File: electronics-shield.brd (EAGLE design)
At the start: 65 x 56 mm, 104 parts, among them IC1 TLE9201SG, IC2 TLE9201SG, IC3 TLE9201SG, IC4 TLE9201SG, IC6 AOZ1232QI-01, IC8 AOZ1232QI-01, Q2 IRFR5305, U1 STM32F0XX8T, U2 EEPROM-I2C, U3 MAXIM_DS3231MZ+MAXIM_DS3231MZ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, U4 V_REG_317SMD, X1 CONNECTOR_PHOENIX_3.81, X2 Listwa zaciskowa rozłączalna 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, X3 C-GRID-04-70553, Y2 8MHz

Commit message: Removed unnecessary stuff, cleaning
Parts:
- removed BT1: 6.8MM_COIN_CELL, SparkFun-Batteries:BATTCON-6.8MM
- removed C18, C25: 22uF/35V, rcl:PANASONIC_B
- removed C20, C26: (no value), Kell Ideas:C0603K
- removed C21, C27, C31, C32: 33uF/10V, rcl:PANASONIC_B
- removed C22, C28: 100n, Kell Ideas:C0603K
- removed C23, C29: 1nF, Kell Ideas:C0603K
- removed C24, C30: 1uF/35V, Kell Ideas:C0603K
- removed IC6, IC8: AOZ1232QI-01, Kell Ideas:AOZ1232QI01
- removed L2, L3: 1uH, rcl:L4532P
- removed R11, R16: 65k, Kell Ideas:R0603
- removed R14, R21: 10k, Kell Ideas:R0603
- removed R15, R22: 100k, Kell Ideas:R0603
- removed R17, R18, R19, R20: (no value), Kell Ideas:R0603
- removed R23, R24: 456, Kell Ideas:R0603
- removed U2: EEPROM-I2C, Kell Ideas:SO-08
- removed U3: MAXIM_DS3231MZ+MAXIM_DS3231MZ+_0_0, Kell Ideas:MAXIM_DS3231MZ+_0
- removed X3: C-GRID-04-70553, con-molex:70553-04
- added U$1, U$2: POLOLU_D24V22FX, Kell Ideas:POLOLU_D24V22FX
- moved F3 5.79 mm to (32.0, 26.2)
- moved F5 2.62 mm to (19.8, 23.9), turned to 0 degrees
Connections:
- net UART_SELECTOR renamed SIGNAL_SELECTOR
- removed net BATTERY: BT1.+
- removed net BST1: C22.2, IC6.27
- removed net BST2: C28.2, IC8.27
- removed net FB1: IC6.5, R11.2, R14.1
- removed net FB2: IC8.5, R16.2, R21.1
- removed net LX2: C28.1, IC8.20, IC8.21, IC8.22, IC8.23, IC8.24, IC8.25, IC8.31, L3.1, R16.1
- removed net LX3: C22.1, IC6.20, IC6.21, IC6.22, IC6.23, IC6.24, IC6.25, IC6.31, L2.1, R11.1
- removed net N$2: R18.1
- removed net N$3: R17.1
- removed net PGOOD1: IC6.1, R15.2
- removed net PGOOD2: IC8.1, R22.2
- removed net SS1: C23.2, IC6.30
- removed net SS2: C29.2, IC8.30
- removed net TON1: IC6.6, R24.2
- removed net TON2: IC8.6, R23.2
- removed net VBAT: U3.6
- removed net VCC_INT1: C24.2, IC6.2, IC6.28, R15.1
- removed net VCC_INT2: C30.2, IC8.2, IC8.28, R22.1
- new net STM_RX: U1.43
- new net STM_TX: U1.42
- net +3V3: no longer C20.1, C26.2, R17.2, R18.2, R19.1, R20.1, U2.7, U2.8
- net +5V: now also U$2.P$5; no longer C27.+, C31.+, L3.2
- net DATA_N: no longer X3.3
- net DATA_P: no longer X3.2
- net GND: now also U$1.P$4, U$2.P$4; no longer BT1.-, C18.-, C20.2, C21.-, C23.1, C24.1, C25.-, C26.1, C27.-, C29.1, C30.1, C31.-, C32.-, IC6.12, IC6.13, IC6.14, IC6.15, IC6.16, IC6.17, IC6.18, IC6.19, IC6.26, IC6.29, IC6.32, IC6.4, IC8.12, IC8.13, IC8.14, IC8.15, IC8.16, IC8.17, IC8.18, IC8.19, IC8.26, IC8.29, IC8.32, IC8.4, R14.2, R21.2, U2.2, U2.3, U2.4, U3.5, X3.1
- net RPI_RXD: no longer U1.42
- net RPI_TXD: no longer U1.43
- net SCL: no longer R19.2, U1.35, U2.6
- net SDA: no longer R20.2, U1.36, U2.5
- net VCC: now also U$1.P$3, U$2.P$3; no longer C18.+, C25.+, IC6.10, IC6.11, IC6.33, IC6.7, IC6.8, IC6.9, IC8.10, IC8.11, IC8.33, IC8.7, IC8.8, IC8.9, R23.1, R24.1, U3.2
- net VCC_SERVO: now also U$1.P$5; no longer C21.+, C32.+, L2.2
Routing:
- net N$18: track 9.74 -> 47.4 mm, vias 0 -> 2
- net DATA_N: track 31.5 -> 0.00 mm
- net DATA_P: track 26.0 -> 0.00 mm
- net VCC: track 152.1 -> 176.2 mm
- net GND: track 23.3 -> 1.52 mm, vias 68 -> 62
- net SDA_RX: track 15.6 -> 0.00 mm
- net SCL: track 25.4 -> 10.6 mm
- net SCL_TX: track 14.6 -> 0.00 mm
- net SDA: track 28.0 -> 13.8 mm
- net VCC_INT2: track 11.3 -> 0.00 mm, vias 2 -> 0
- net VCC_INT1: track 11.3 -> 0.00 mm, vias 2 -> 0
- net VCC_SERVO: track 35.2 -> 46.1 mm
- net RPI_TXD: track 27.4 -> 19.4 mm
- net RPI_RXD: track 22.4 -> 14.7 mm
- net LX2: track 7.38 -> 0.00 mm, vias 2 -> 0
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- removed copper zone on layer 16, net +5V
- removed copper zone on layer 16, net LX2
- removed copper zone on layer 16, net LX3
- removed copper zone on layer 16, net VCC
- removed copper zone on layer 16, net VCC_SERVO
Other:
- board text added: "POLOLU D24V22Fx 5V"
- board text added: "POLOLU D24V22Fx 6V/9V/12V"
- board text added: "electronics-shield ver 8 2018 Kell ideas Ltd."
- board text removed: "electronics-shield ver 8 rev A 2018 Kell ideas Ltd."

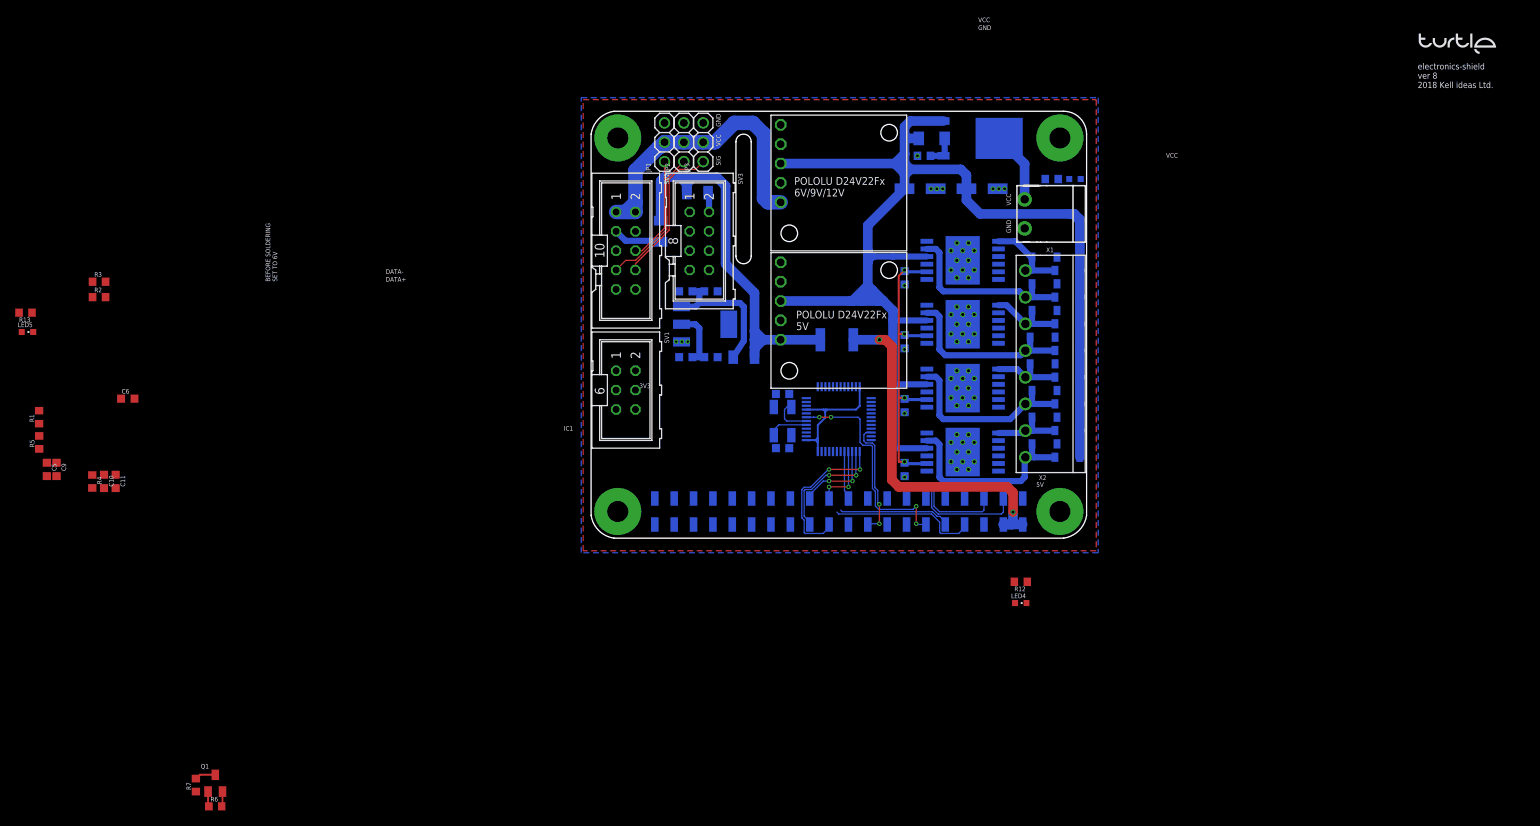
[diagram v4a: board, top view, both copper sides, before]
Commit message: Basic placement of rest of components
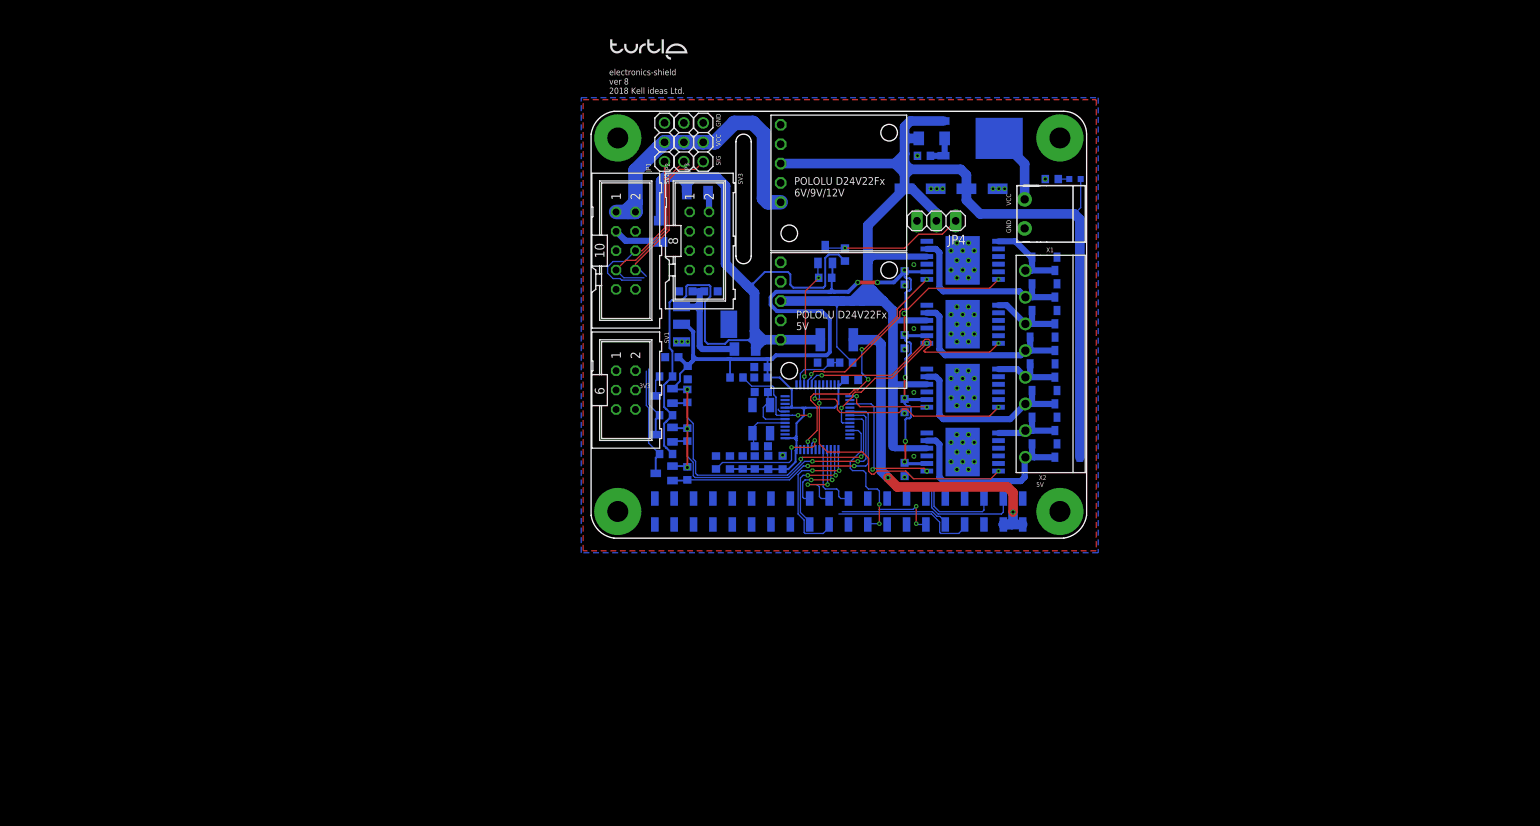
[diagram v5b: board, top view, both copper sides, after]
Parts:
- removed LED4, LED5: LEDCHIPLED_0603, audio amplifier example:CHIPLED_0603
- added JP4: (no value), pinhead:1X03
- added Q3, Q4, Q5: (no value), adafruit:SOT23
- added R10, R11, R14, R15, R16, R17: 10k, rcl:R0603
- moved R13 105.0 mm to (30.3, 23.2), flipped to the bottom, turned to 0 degrees
- moved C9 95.3 mm to (24.9, 10.1), flipped to the bottom, turned to 90 degrees
- moved C6 95.0 mm to (33.9, 20.9), flipped to the bottom, turned to 180 degrees
- moved C5 94.6 mm to (23.0, 10.1), flipped to the bottom, turned to 90 degrees
- moved R1 94.1 mm to (21.2, 10.1), flipped to the bottom, turned to 270 degrees
- moved R5 88.8 mm to (16.2, 10.1), flipped to the bottom, turned to 270 degrees
- moved R3 87.7 mm to (19.7, 10.1), flipped to the bottom, turned to 270 degrees
- moved C10 87.5 mm to (22.0, 22.6), flipped to the bottom, turned to 0 degrees
- moved C11 85.7 mm to (22.0, 21.2), flipped to the bottom, turned to 0 degrees
- moved R4 85.6 mm to (18.8, 21.2), flipped to the bottom, turned to 0 degrees
- moved R2 85.5 mm to (18.0, 10.1), flipped to the bottom, turned to 270 degrees
- moved R6 75.8 mm to (12.4, 8.64), flipped to the bottom, turned to 270 degrees
- moved R7 75.4 mm to (9.60, 11.2), flipped to the bottom, turned to 0 degrees
- moved Q1 71.5 mm to (9.35, 8.64), flipped to the bottom, turned to 270 degrees
- moved R12 36.8 mm to (33.2, 23.2), flipped to the bottom, turned to 0 degrees
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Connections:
- net DATA_N renamed NSS_1
- net DATA_P renamed NSS_2
- removed net N$4: LED4.C, R12.1
- removed net N$5: LED5.C, R13.1
- removed net SO1-SI3: IC1.3, IC3.8
- removed net SO2-SI4: IC2.3, IC4.8
- removed net SO3-SI2: IC2.8, IC3.3
- new net LED_5V: JP4.1, Q5.3, R17.2
- net +3V3: now also Q3.1, Q4.1, Q5.1, R10.1, R14.1, R16.1; no longer LED5.A
- net +5V: now also R11.1, R15.1, R17.1; no longer LED4.A
- net BAT_MEAS: now also R12.2, R13.1
- net GND: now also IC1.10, IC1.3, IC1.8, IC1.9, IC2.10, IC2.3, IC2.8, IC2.9, IC3.10, IC3.3, IC3.8, IC3.9, IC4.10, IC4.3, IC4.8, IC4.9, JP4.3; no longer R12.2
- net LED: now also Q5.2, R16.2
- net RPI_CLK: no longer IC1.10, IC2.10, IC3.10, IC4.10
- net RPI_MISO: no longer IC4.3
- net RPI_MOSI: no longer IC1.8
- net SERVO1: now also Q1.3, R7.2
- net SERVO1_UC: now also Q1.2, R6.2
- net SERVO2: now also Q3.3, R11.2; no longer Q1.3, R7.2
- net SERVO2_UC: now also Q3.2, R10.2; no longer Q1.2, R6.2
- net SERVO3: now also Q4.3, R15.2
- net SERVO3_UC: now also Q4.2, R14.2
- net TLE_NSS: no longer IC1.9, IC2.9, IC3.9, IC4.9
- net VCC: now also JP4.2, R12.1
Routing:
- net +3V3: track 69.7 -> 169.7 mm, vias 4 -> 12
- net +5V: track 56.0 -> 121.6 mm
- net SERVO3_UC: track 0.00 -> 41.5 mm, vias 0 -> 2
- net SERVO2_UC: track 1.99 -> 38.3 mm, vias 0 -> 2
- net SERVO1_UC: track 0.00 -> 35.7 mm, vias 0 -> 2
- net EN4: track 0.00 -> 34.9 mm, vias 0 -> 2
- net IN11: track 0.00 -> 33.5 mm, vias 0 -> 4
- net EN1: track 0.00 -> 31.8 mm, vias 0 -> 2
- net EN2: track 0.00 -> 30.8 mm, vias 0 -> 2
- net EN3: track 0.00 -> 28.4 mm, vias 0 -> 2
- net SERVO1: track 13.8 -> 38.3 mm
- net VCC: track 176.2 -> 197.5 mm
- net IN41: track 0.00 -> 18.9 mm, vias 0 -> 3
- net LED_5V: track 0.00 -> 18.7 mm, vias 0 -> 1
- net IN21: track 0.00 -> 17.9 mm, vias 0 -> 2
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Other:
- board text removed: "BEFORE SOLDERING SET TO 6V"
- board text removed: "DATA+"
- board text removed: "DATA-"
- board text removed: "IC1"

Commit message: Finish wiring, DRC done
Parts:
- added U2, U3: NC7SV157P6X, Kell Ideas:SOT65P210X110-6N
- moved R3 1.83 mm to (17.8, 10.1)
- moved R2 1.68 mm to (19.7, 10.1)
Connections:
- removed net SCL: PCB1.5, R3.1
- removed net SDA: PCB1.3, R2.1
- net +3V3: now also U2.5, U3.5
- net GND: now also U2.2, U3.2
- net NSS_1: now also PCB1.24, U1.38
- net RPI_RXD: now also U3.4
- net RPI_TXD: now also U2.4
- net SCL_TX: now also PCB1.5, R3.1, U2.1; no longer U1.21
- net SDA_RX: now also PCB1.3, R2.1, U3.1; no longer U1.22
- net SIGNAL_SELECTOR: now also U2.6, U3.6
- net SPI1_NSS: no longer PCB1.24, U1.38
- net STM_RX: now also U2.3
- net STM_TX: now also U3.3
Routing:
- net SDA_RX: track 0.00 -> 104.8 mm, vias 0 -> 5
- net SCL_TX: track 0.00 -> 92.9 mm, vias 0 -> 5
- net NSS_1: track 0.00 -> 89.9 mm, vias 0 -> 2
- net RPI_MOSI: track 9.27 -> 79.7 mm, vias 0 -> 1
- net RPI_MISO: track 11.5 -> 72.5 mm, vias 2 -> 3
- net RPI_CLK: track 11.1 -> 69.6 mm, vias 2 -> 3
- net SWDIO: track 18.8 -> 75.2 mm, vias 2 -> 3
- net SIGNAL_SELECTOR: track 0.00 -> 48.2 mm, vias 0 -> 6
- net SWCLK: track 20.4 -> 61.5 mm, vias 2 -> 3
- net RPI_RXD: track 14.4 -> 50.6 mm
- net NRST: track 21.5 -> 57.4 mm, vias 4 -> 7
- net RPI_TXD: track 19.1 -> 49.9 mm
- net STM_TX: track 0.00 -> 20.6 mm, vias 0 -> 2
- net +3V3: track 169.7 -> 189.3 mm
- net STM_RX: track 0.00 -> 16.0 mm, vias 0 -> 2
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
